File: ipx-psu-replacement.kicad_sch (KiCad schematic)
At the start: 31 parts, among them J1 L, J10 -12V, J11 GND, J12 Fan, J13 SENS, J14 GND, J15 GND, J2 AC IN, J3 GND, J4 Floppy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

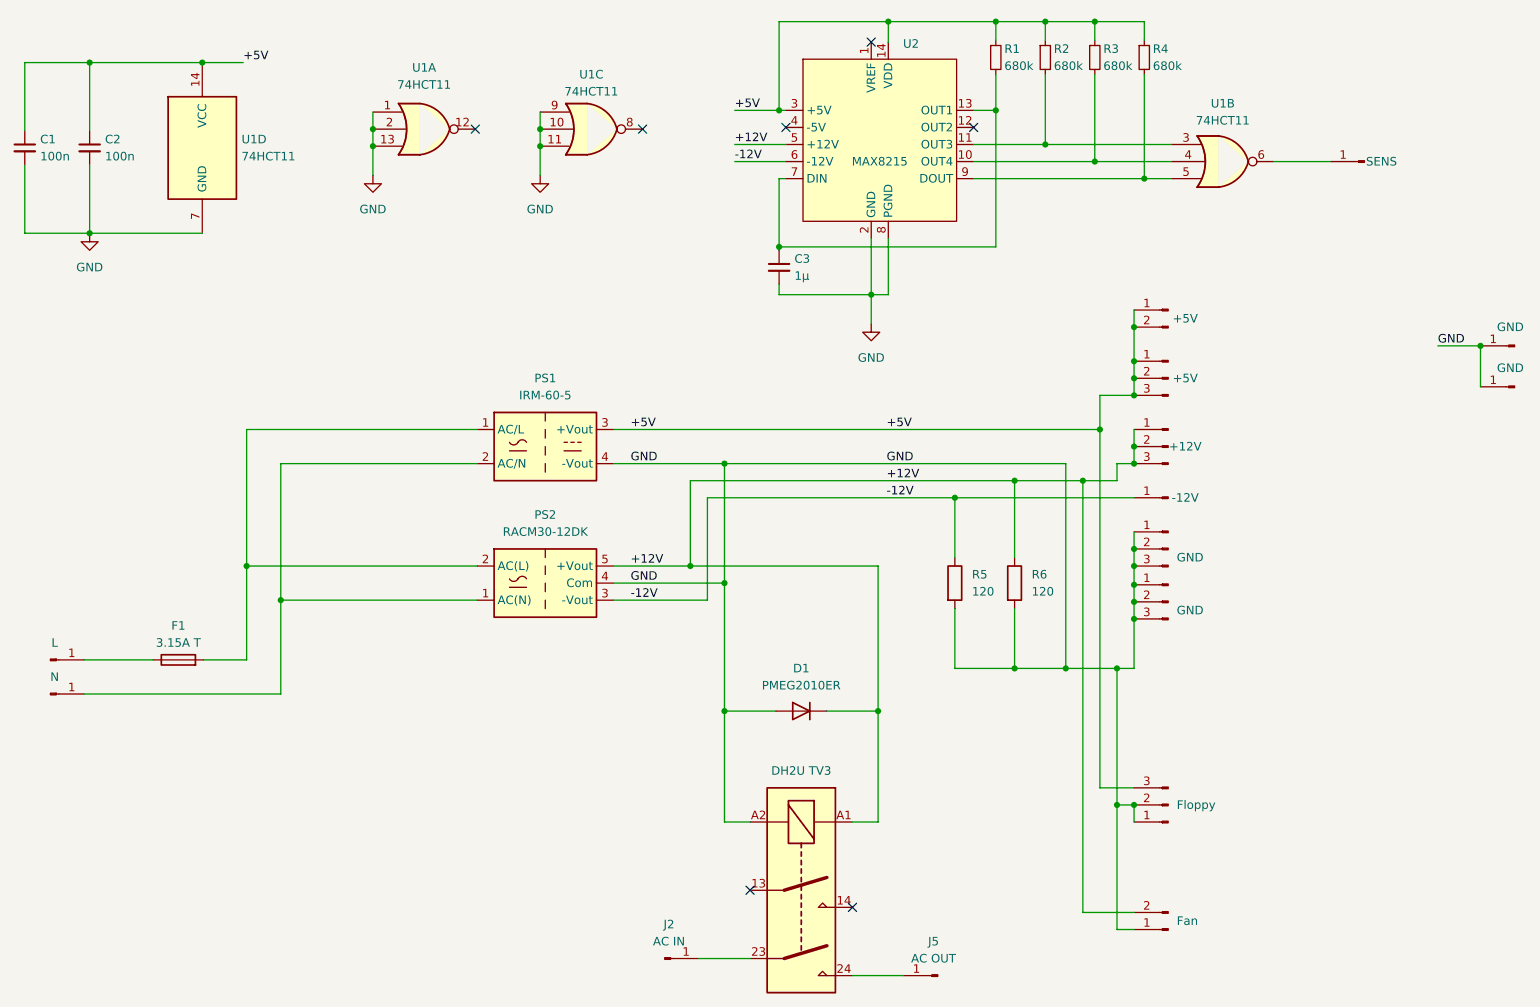
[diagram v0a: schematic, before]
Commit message: Fix U1 schematic symbol and flyback diode description
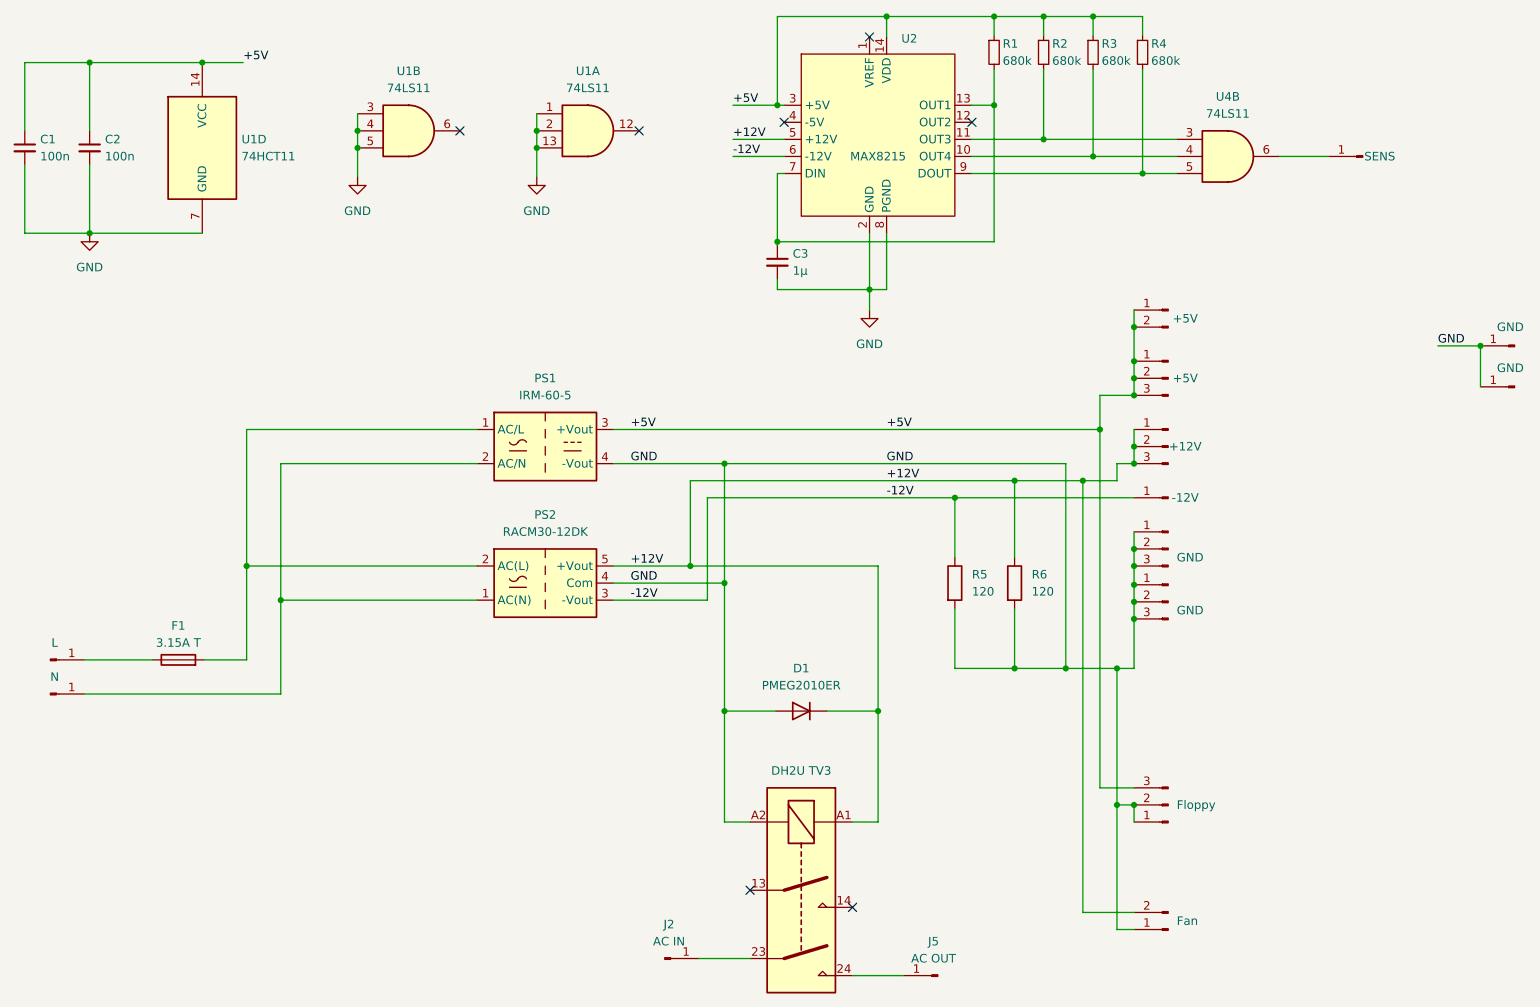
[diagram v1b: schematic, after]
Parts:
- removed unit 3 of U1
- removed unit 2 of U1
- removed unit 1 of U1
- added unit 1 of U1
- added unit 2 of U1
- added U4: 74LS11, symbol 74xx:74LS11
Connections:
- net GND: now also U1.1, U1.13, U1.2, U1.3, U1.4, U1.5
- net at J13.1 (Pin_1): now also U4.6
- net at R4.2, U2.9 (DOUT): now also U4.5
- net at R3.2, U2.10 (OUT4): now also U4.4
- net at R2.2, U2.11 (OUT3): now also U4.3
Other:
- moved on the sheet: C3, R1, R2, R3, R4, U2
